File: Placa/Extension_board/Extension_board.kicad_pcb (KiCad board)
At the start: 2 copper layers, 40.6 x 20.3 mm, 8 parts, among them J1 USB_B_Micro, J2 USB_B_Micro, J3 Conn_01x04_Male, U1 STEVAL-STLCS01V1

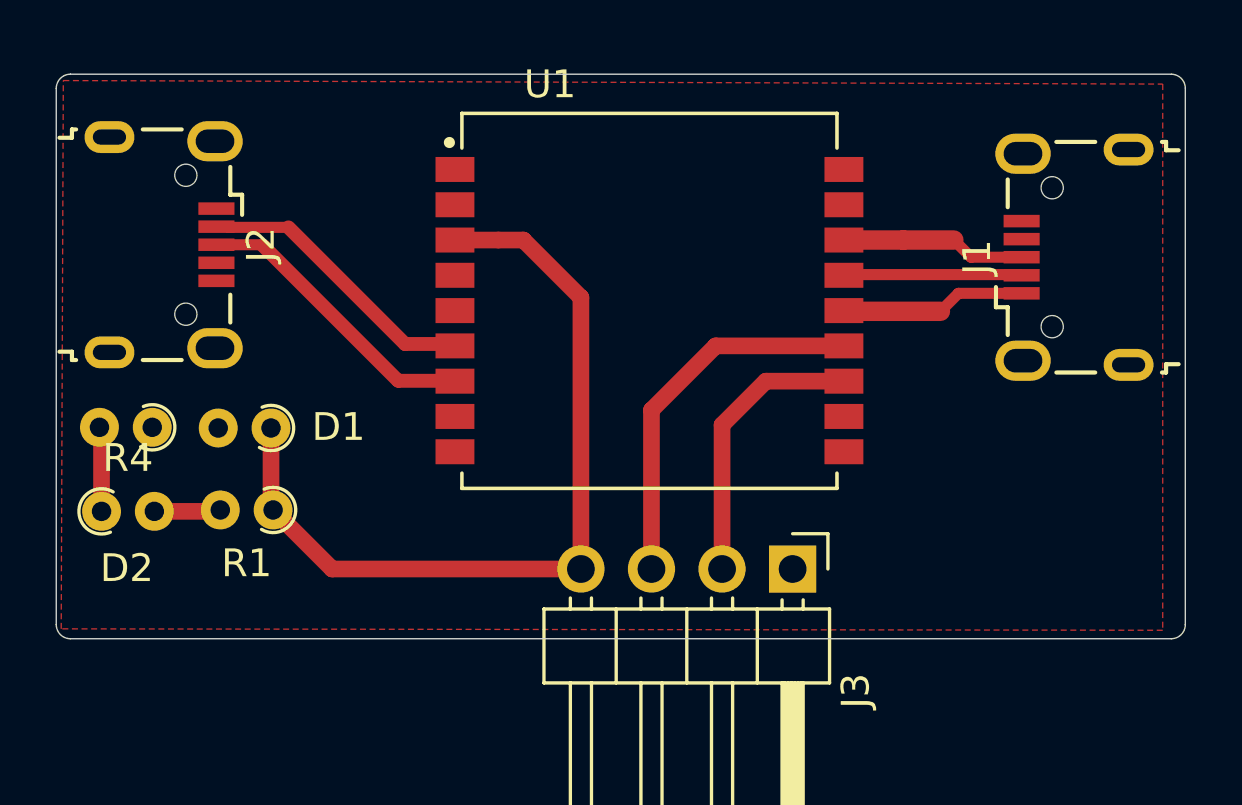
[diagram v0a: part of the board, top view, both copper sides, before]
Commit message: Cambio de footprint usb
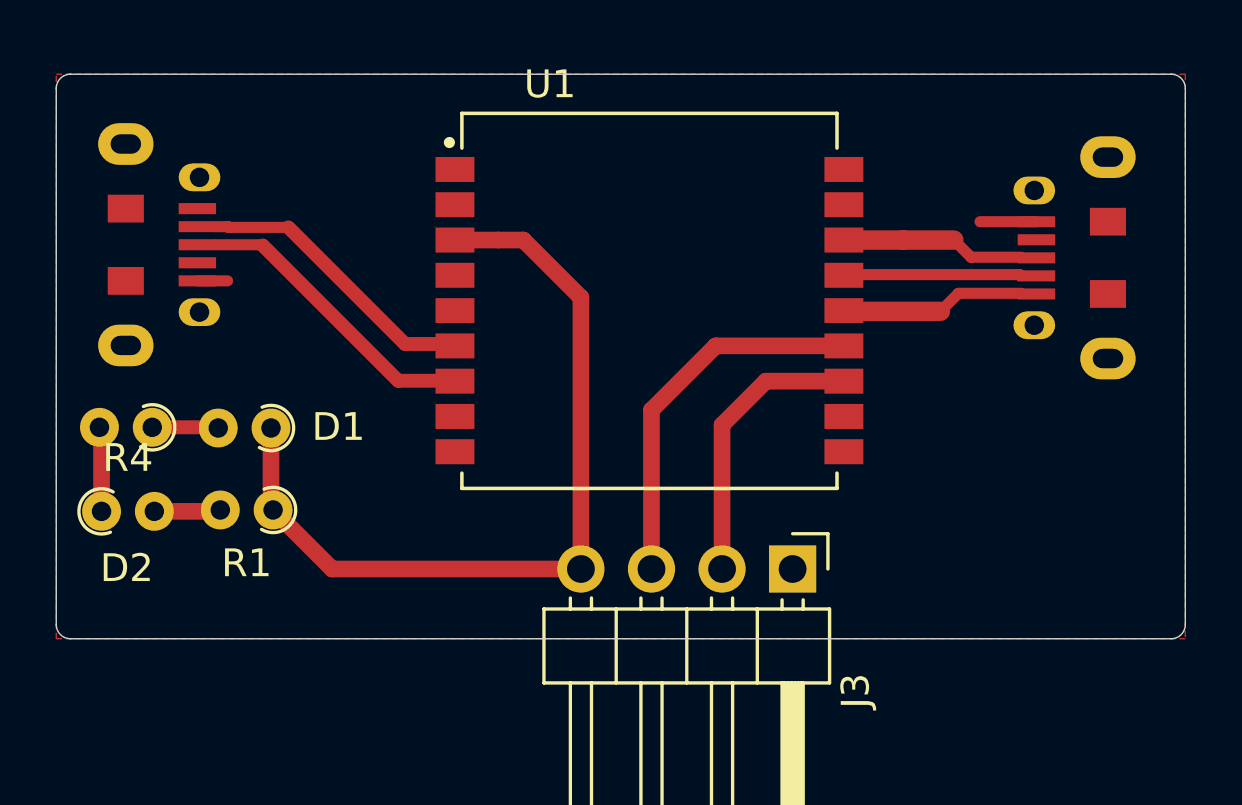
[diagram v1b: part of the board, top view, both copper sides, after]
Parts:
- J1, J2: footprint Connector_USB:USB_Micro-B_Wuerth_629105150521 -> freetronics_footprints:USB-MICRO-5pin_PTHMOUNT
- moved J1 1.37 mm to (131.8, 53.6), turned to 180 degrees
- moved J2 1.21 mm to (101.6, 53.1), turned to 0 degrees
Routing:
- net /GND: track 0.00 -> 5.68 mm

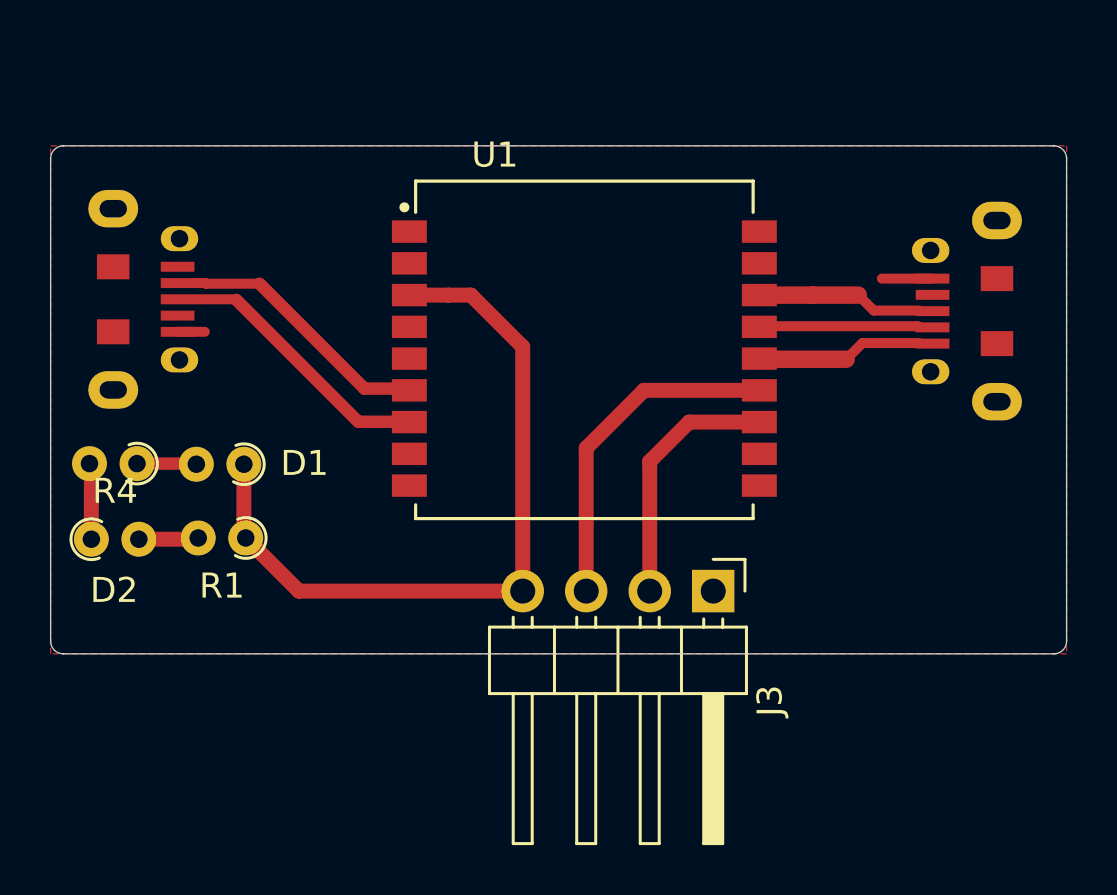
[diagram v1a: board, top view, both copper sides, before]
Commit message: Ampliacion de los pads de los componentes
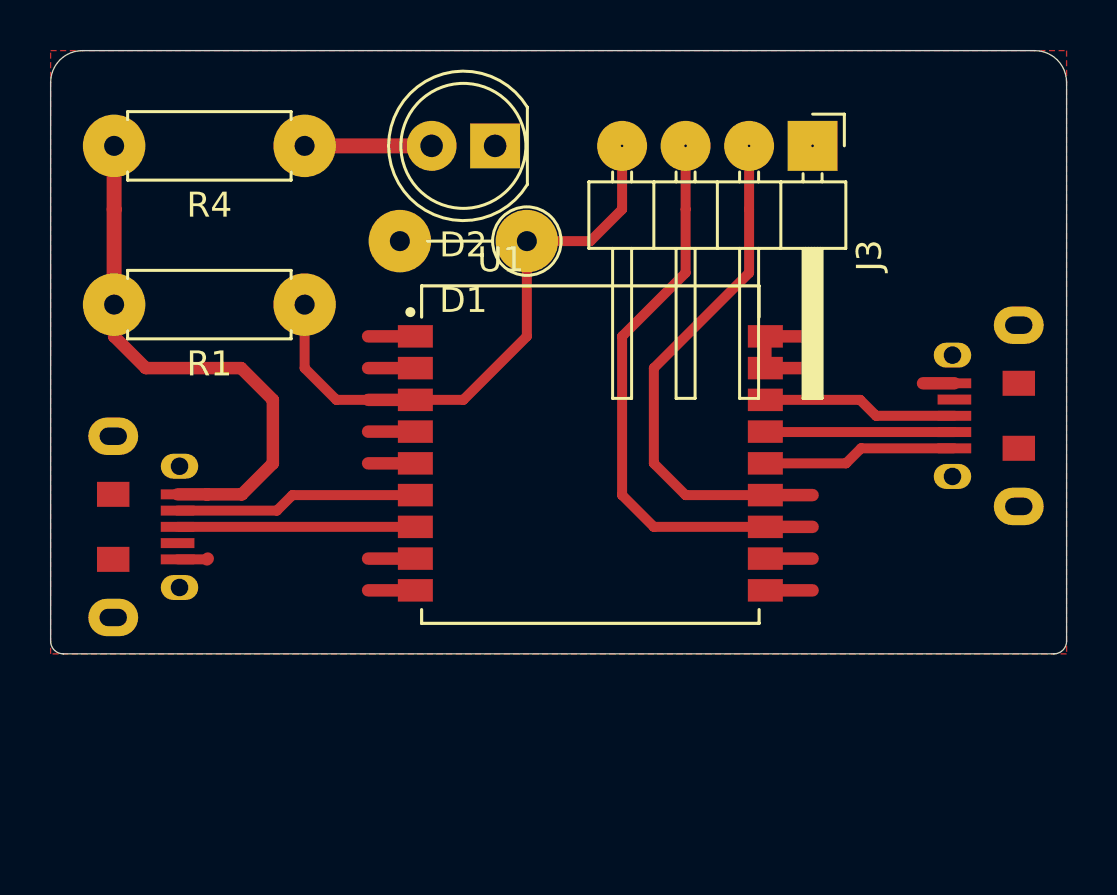
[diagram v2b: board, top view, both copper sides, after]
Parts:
- D1: footprint Resistor_THT:R_Axial_DIN0204_L3.6mm_D1.6mm_P1.90mm_Vertical -> Resistor_THT:R_Axial_DIN0207_L6.3mm_D2.5mm_P5.08mm_Vertical
- D2: footprint Resistor_THT:R_Axial_DIN0204_L3.6mm_D1.6mm_P1.90mm_Vertical -> LED_THT:LED_D5.0mm_IRBlack
- R1, R4: footprint Resistor_THT:R_Axial_DIN0204_L3.6mm_D1.6mm_P1.90mm_Vertical -> Resistor_THT:R_Axial_DIN0207_L6.3mm_D2.5mm_P7.62mm_Horizontal
- moved D2 19.2 mm to (114.3, 47.0)
- moved J3 18.2 mm to (127.0, 47.0)
- moved R4 17.9 mm to (106.7, 47.0), turned to 180 degrees
- moved D1 14.4 mm to (115.6, 50.8)
- moved R1 9.63 mm to (106.7, 53.3)
- moved J2 9.10 mm to (101.6, 62.2)
- moved J1 4.28 mm to (132.7, 57.8)
- moved U1 4.20 mm to (118.1, 59.7)
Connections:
- J3 pad 2: /I2C_SDA -> /I2C_SCL
- J3 pad 3: /I2C_SCL -> /I2C_SDA
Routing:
- net /V_USB: track 2.40 -> 21.9 mm
- net /I2C_SDA: track 10.2 -> 23.2 mm
- net /I2C_SCL: track 13.6 -> 21.2 mm
- net /VIN: track 30.1 -> 23.7 mm
- net /GND: track 5.68 -> 9.41 mm
- net Net-(D2-Pad2): track 3.06 -> 5.08 mm
- net Net-(U1-Pad9): track 0.00 -> 1.89 mm
- net Net-(U1-Pad8): track 0.00 -> 1.89 mm
- net Net-(U1-Pad4): track 0.00 -> 1.89 mm
- net Net-(U1-Pad2): track 0.00 -> 1.89 mm
- net Net-(U1-Pad11): track 0.00 -> 1.89 mm
- net Net-(U1-Pad10): track 0.00 -> 1.89 mm
- net Net-(U1-Pad1): track 0.00 -> 1.89 mm
- net /SWDIO: track 6.65 -> 7.83 mm
- net /SWDCLK: track 6.42 -> 7.57 mm
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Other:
- board size 40.6 x 20.3 mm -> 40.6 x 24.1 mm

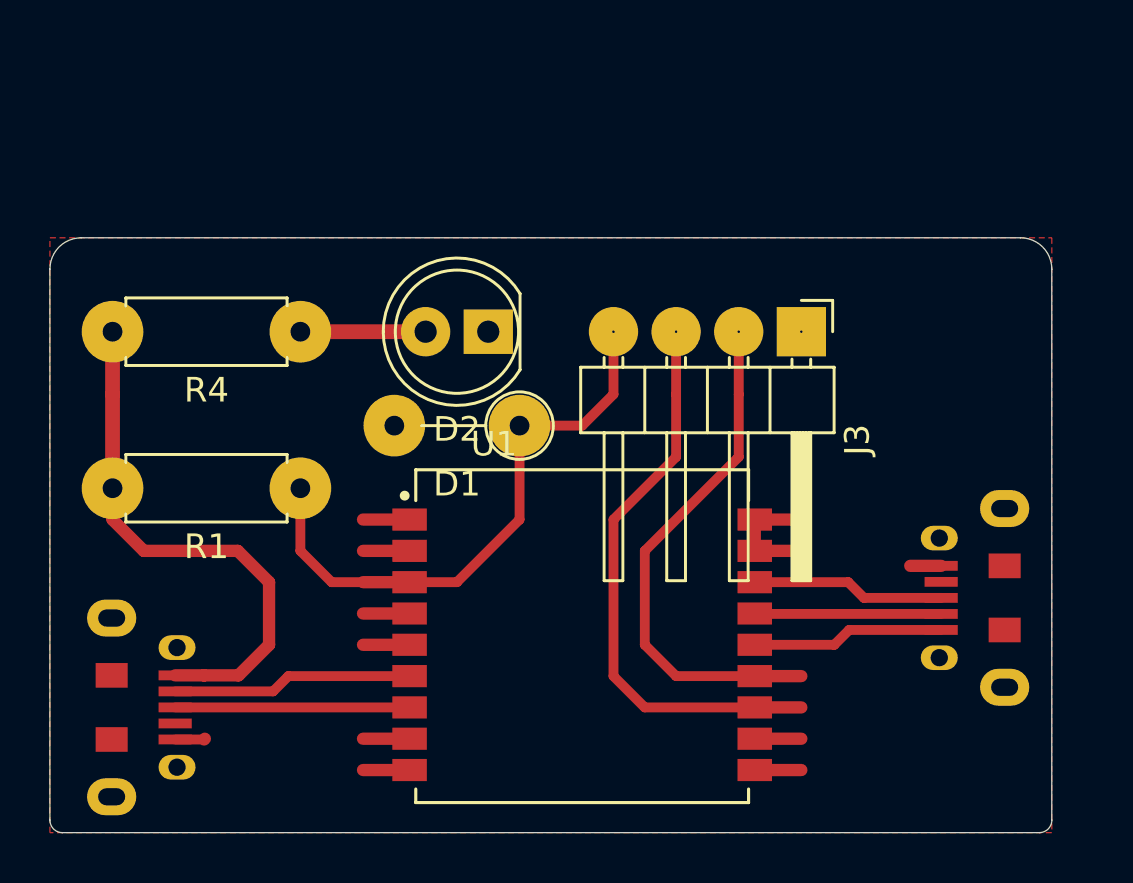
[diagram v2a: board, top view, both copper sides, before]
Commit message: Agregado de nuevos pines en I2C
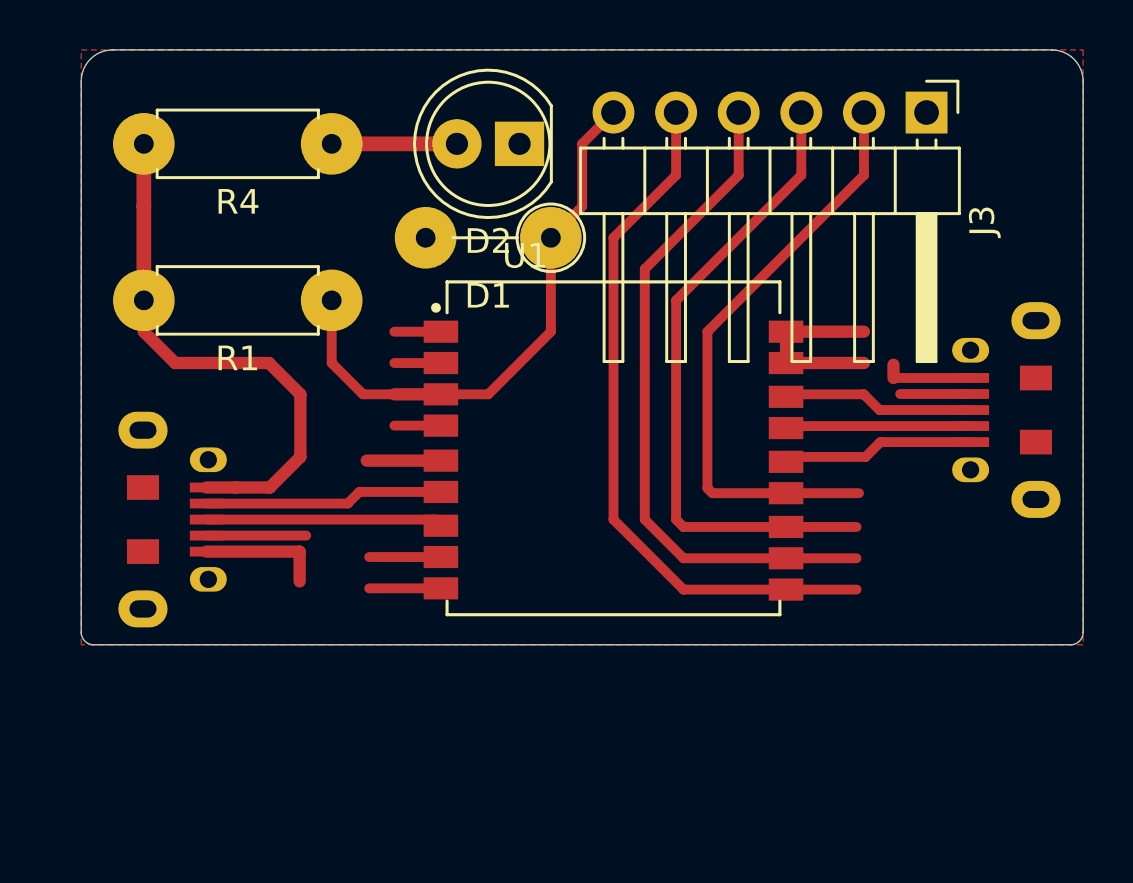
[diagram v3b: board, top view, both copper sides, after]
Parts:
- J3: value Conn_01x04_Male -> Conn_01x06_Male; footprint Connector_PinHeader_2.54mm:PinHeader_1x04_P2.54mm_Horizontal -> Connector_PinHeader_2.54mm:PinHeader_1x06_P2.54mm_Horizontal
- moved J3 10.2 mm to (132.1, 38.1)
- moved D2 7.73 mm to (115.6, 39.4)
- moved R1 7.73 mm to (108.0, 45.7)
- moved R4 7.73 mm to (108.0, 39.4)
- moved D1 7.73 mm to (116.8, 43.2)
- moved J1 7.73 mm to (133.9, 50.2)
- moved J2 7.73 mm to (102.9, 54.6)
- moved U1 7.73 mm to (119.4, 52.1)
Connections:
- J3 pad 4: /VIN -> /SAI_SD
- U1 pad 10: Net-(U1-Pad10) -> /SAI_MCLK
- U1 pad 11: Net-(U1-Pad11) -> /SAI_SD
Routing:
- net /SAI_MCLK: track 0.00 -> 28.6 mm
- net /SAI_SD: track 0.00 -> 27.3 mm
- net /GND: track 9.41 -> 19.3 mm
- net Net-(J2-Pad4): track 0.00 -> 4.05 mm
- net /I2C_SCL: track 21.2 -> 24.1 mm
- net Net-(J1-Pad4): track 0.00 -> 2.93 mm
- net /I2C_SDA: track 23.2 -> 26.1 mm
- net Net-(U1-Pad11): track 1.89 -> 0.00 mm
- net Net-(U1-Pad10): track 1.89 -> 0.00 mm
- net Net-(U1-Pad9): track 1.89 -> 2.91 mm
- net Net-(U1-Pad8): track 1.89 -> 2.91 mm
- net /VIN: track 23.7 -> 23.0 mm

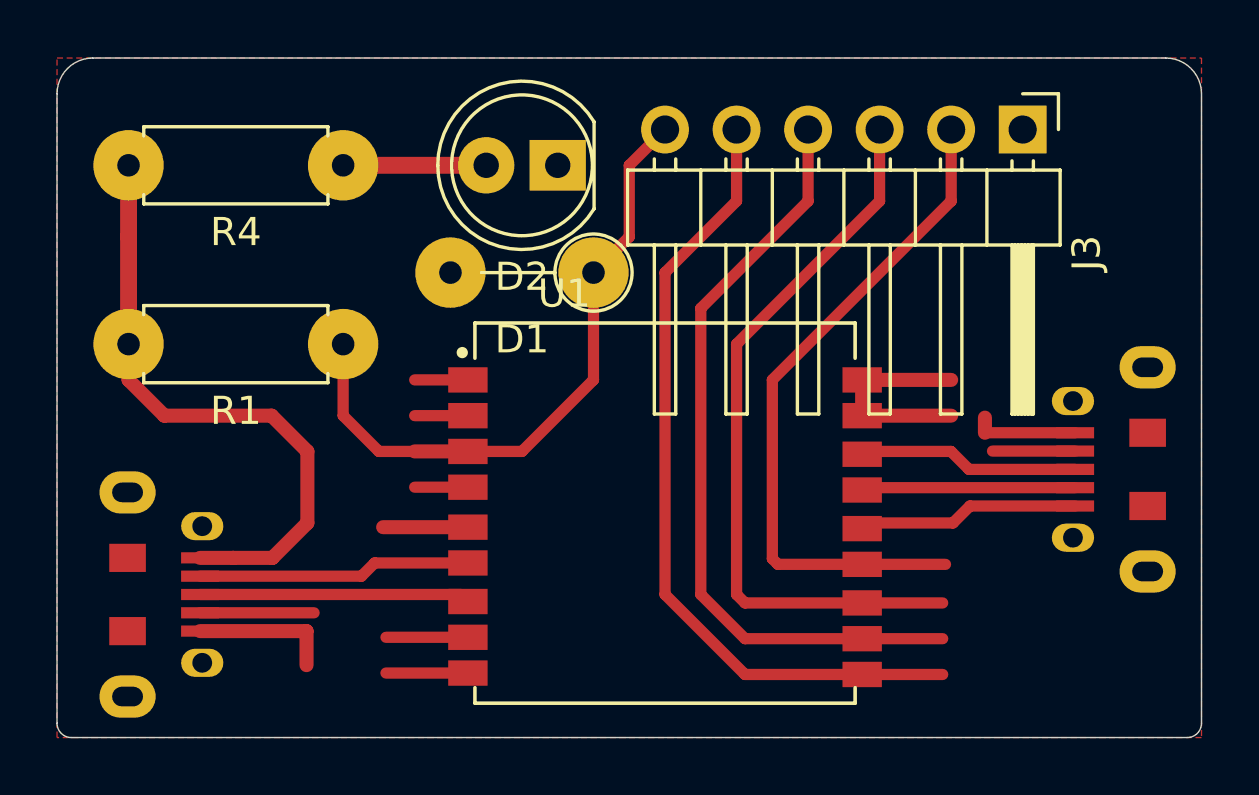
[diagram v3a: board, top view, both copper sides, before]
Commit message: Correccion de errores en pads y pistas
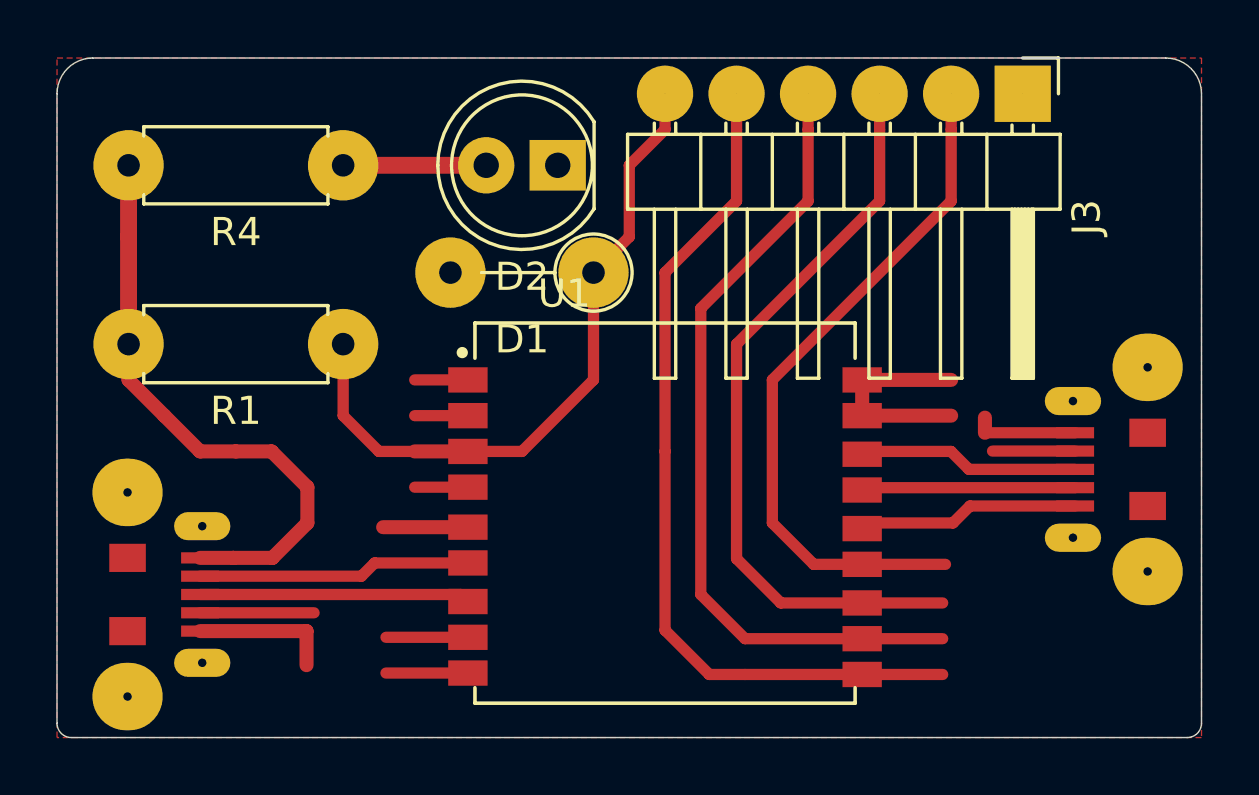
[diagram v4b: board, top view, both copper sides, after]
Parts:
- R1: value 1,2Ω -> 12Ω
- moved J3 1.27 mm to (132.1, 36.8)
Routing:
- net /SAI_MCLK: track 28.6 -> 30.6 mm
- net /VIN: track 23.0 -> 24.2 mm
- net /SAI_SD: track 27.3 -> 28.6 mm
- net /V_USB: track 21.9 -> 21.1 mm
- net /I2C_SDA: track 26.1 -> 26.6 mm
- net /I2C_SCL: track 24.1 -> 24.6 mm

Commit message: Revision
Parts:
- added C1: C, Capacitor_SMD:C_0805_2012Metric, F.Cu at (141.0, 86.4)
- added SW1: SW_PUSHBUTTON, Button_Switch_THT:SW_PUSH_6mm_H5mm, F.Cu at (146.7, 83.2)
- moved J1 31.4 mm to (152.4, 75.6)
- moved D1 29.6 mm to (132.1, 68.6)
- moved D2 29.6 mm to (130.8, 64.8)
- moved U1 29.6 mm to (134.6, 77.5)
- moved R1 29.6 mm to (123.2, 71.1)
- moved R4 29.6 mm to (123.2, 64.8)
- moved J3 29.6 mm to (147.3, 62.2)
- moved J2 28.4 mm to (115.6, 80.0)
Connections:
- J2 pad 2: /RXD-USB_DP -> /RXD-USB_DM
- J2 pad 3: /RXD-USB_DM -> /RXD-USB_DP
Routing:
- net /RESET: track 7.89 -> 36.2 mm
- net /RXD-USB_DP: track 9.70 -> 28.9 mm
- net (no net): track 0.00 -> 16.9 mm
- net /GND: track 19.3 -> 22.5 mm
- net /SWDCLK: track 7.57 -> 10.8 mm
- net Net-(J1-Pad4): track 2.93 -> 6.15 mm
- net /SWDIO: track 7.87 -> 11.1 mm
- net /RXD-USB_DM: track 9.61 -> 12.8 mm
- net /V_USB: track 21.1 -> 21.7 mm
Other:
- board size 40.6 x 24.1 mm -> 47 x 29.2 mm
